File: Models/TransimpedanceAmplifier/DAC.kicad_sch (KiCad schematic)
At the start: 11 parts, among them U10 DAC81401

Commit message: Finalized the last detail of the schematic
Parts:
- renumbered R17 to R18
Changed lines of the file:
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@@
 		(dnp no)
 		(fields_autoplaced yes)
-		(property "Reference" "R17"
+		(property "Reference" "R18"
 			(at 143.51 36.83 90)
 			(effects
@@
 			(project ""
 				(path "/ec9f2ae3-e40d-40eb-9760-2b611ee8efd1/7e303428-a18c-4ad4-b002-5ab9c6631588/77c98efe-b6d0-43b4-bfa9-b392bfbf9a85"
-					(reference "R17")
+					(reference "R18")
 					(unit 1)
 				)

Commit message: Working on filling in the last details of the schematics
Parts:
- C25, C26, C27, C28, C29: footprint (none) -> TwoTerminal:CAPC0603; Cost (none) -> $0.00; RoHS Compliant (none) -> NO
- NT1, NT2, NT3, NT4, R18, U10: Cost (none) -> $0.00; RoHS Compliant (none) -> NO
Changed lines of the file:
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@@
 			)
 		)
-		(property "Footprint" ""
+		(property "Footprint" "TwoTerminal:CAPC0603"
 			(at 51.7652 114.3 0)
 			(effects
@@
 		)
 		(property "Purchase Link" "https://www.digikey.com/en/products/detail/murata-electronics/GRT188R61H105KE13D/5416752"
+			(at 50.8 110.49 0)
+			(effects
+				(font
+					(size 1.27 1.27)
+				)
+				(hide yes)
+			)
+		)
+		(property "Cost" "$0.00"
+			(at 50.8 110.49 0)
+			(effects
+				(font
+					(size 1.27 1.27)
+				)
+				(hide yes)
+			)
+		)
+		(property "RoHS Compliant" "NO"
 			(at 50.8 110.49 0)
 			(effects
@@
 			)
 		)
-		(property "Footprint" ""
+		(property "Footprint" "TwoTerminal:CAPC0603"
 			(at 127.9652 165.1 0)
 			(effects
@@
 		)
 		(property "Purchase Link" "https://www.digikey.com/en/products/detail/murata-electronics/GRT188R61H105KE13D/5416752"
+			(at 127 161.29 0)
+			(effects
+				(font
+					(size 1.27 1.27)
+				)
+				(hide yes)
+			)
+		)
+		(property "Cost" "$0.00"
+			(at 127 161.29 0)
+			(effects
+				(font
+					(size 1.27 1.27)
+				)
+				(hide yes)
+			)
+		)
+		(property "RoHS Compliant" "NO"
 			(at 127 161.29 0)
 			(effects
@@
 			)
 		)
+		(property "Cost" "$0.00"
+			(at 58.42 152.4 0)
+			(effects
+				(font
+					(size 1.27 1.27)
+				)
+				(hide yes)
+			)
+		)
+		(property "RoHS Compliant" "NO"
+			(at 58.42 152.4 0)
+			(effects
+				(font
+					(size 1.27 1.27)
+				)
+				(hide yes)
+			)
+		)
 		(pin "2"
 		)
@@
 			)
 		)
-		(property "Footprint" ""
+		(property "Footprint" "TwoTerminal:CAPC0603"
 			(at 127.9652 114.3 0)
 			(effects
@@
 		)
 		(property "Purchase Link" "https://www.digikey.com/en/products/detail/murata-electronics/GRT188R61H105KE13D/5416752"
+			(at 127 110.49 0)
+			(effects
+				(font
+					(size 1.27 1.27)
+				)
+				(hide yes)
+			)
+		)
+		(property "Cost" "$0.00"
+			(at 127 110.49 0)
+			(effects
+				(font
+					(size 1.27 1.27)
+				)
+				(hide yes)
+			)
+		)
+		(property "RoHS Compliant" "NO"
 			(at 127 110.49 0)
 			(effects
@@
 			)
 		)
+		(property "Cost" "$0.00"
+			(at 143.51 43.18 90)
+			(effects
+				(font
+					(size 1.27 1.27)
+				)
+				(hide yes)
+			)
+		)
+		(property "RoHS Compliant" "NO"
+			(at 143.51 43.18 90)
+			(effects
+				(font
+					(size 1.27 1.27)
+				)
+				(hide yes)
+			)
+		)
 		(pin "1"
 		)
@@
 			)
 		)
+		(property "Cost" "$0.00"
+			(at 58.42 101.6 0)
+			(effects
+				(font
+					(size 1.27 1.27)
+				)
+				(hide yes)
+			)
+		)
+		(property "RoHS Compliant" "NO"
+			(at 58.42 101.6 0)
+			(effects
+				(font
+					(size 1.27 1.27)
+				)
+				(hide yes)
+			)
+		)
 		(pin "2"
 		)
@@
 			)
 		)
+		(property "Cost" "$0.00"
+			(at 134.62 152.4 0)
+			(effects
+				(font
+					(size 1.27 1.27)
+				)
+				(hide yes)
+			)
+		)
+		(property "RoHS Compliant" "NO"
+			(at 134.62 152.4 0)
+			(effects
+				(font
+					(size 1.27 1.27)
+				)
+				(hide yes)
+			)
+		)
 		(pin "2"
 		)
@@
 			)
 		)
-		(property "Footprint" ""
+		(property "Footprint" "TwoTerminal:CAPC0603"
 			(at 44.1452 53.34 0)
 			(effects
@@
 		)
 		(property "Purchase Link" "https://www.digikey.com/en/products/detail/murata-electronics/GRM188R71H224KAC4D/5797498"
+			(at 43.18 49.53 0)
+			(effects
+				(font
+					(size 1.27 1.27)
+				)
+				(hide yes)
+			)
+		)
+		(property "Cost" "$0.00"
+			(at 43.18 49.53 0)
+			(effects
+				(font
+					(size 1.27 1.27)
+				)
+				(hide yes)
+			)
+		)
+		(property "RoHS Compliant" "NO"
 			(at 43.18 49.53 0)
 			(effects
@@
 			)
 		)
+		(property "Cost" "$0.00"
+			(at 134.62 101.6 0)
+			(effects
+				(font
+					(size 1.27 1.27)
+				)
+				(hide yes)
+			)
+		)
+		(property "RoHS Compliant" "NO"
+			(at 134.62 101.6 0)
+			(effects
+				(font
+					(size 1.27 1.27)
+				)
+				(hide yes)
+			)
+		)
 		(pin "1"
 		)
@@
 			)
 		)
+		(property "Cost" "$0.00"
+			(at 72.39 30.48 0)
+			(effects
+				(font
+					(size 1.27 1.27)
+				)
+				(hide yes)
+			)
+		)
+		(property "RoHS Compliant" "NO"
+			(at 72.39 30.48 0)
+			(effects
+				(font
+					(size 1.27 1.27)
+				)
+				(hide yes)
+			)
+		)
 		(pin "13"
 		)
@@
 			)
 		)
-		(property "Footprint" ""
+		(property "Footprint" "TwoTerminal:CAPC0603"
 			(at 51.7652 165.1 0)
 			(effects
@@
 			(at 50.8 161.29 0)
 			(effects
+				(font
+					(size 1.27 1.27)
+				)
+				(hide yes)
+			)
+		)
+		(property "Cost" "$0.00"
+			(at 50.8 161.29 0)
+			(effects
+				(font
+					(size 1.27 1.27)
+				)
+				(hide yes)
+			)
+		)
+		(property "RoHS Compliant" "NO"
+			(at 50.8 161.29 0)
+			(effects

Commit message: Fixed a bug in footprint assignment
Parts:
- NT1, NT2, NT3, NT4: footprint (none) -> Connector_Custom:NetTie_0.2mm
- R18: footprint (none) -> TwoTerminal:RESC0603
- U10: footprint (none) -> IC:DAC81401
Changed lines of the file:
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@@
 			)
 		)
-		(property "Footprint" ""
+		(property "Footprint" "Connector_Custom:NetTie_0.2mm"
 			(at 58.42 152.4 0)
 			(effects
@@
 			)
 		)
-		(property "Footprint" ""
+		(property "Footprint" "TwoTerminal:RESC0603"
 			(at 143.764 42.164 90)
 			(effects
@@
 			)
 		)
-		(property "Footprint" ""
+		(property "Footprint" "Connector_Custom:NetTie_0.2mm"
 			(at 58.42 101.6 0)
 			(effects
@@
 			)
 		)
-		(property "Footprint" ""
+		(property "Footprint" "Connector_Custom:NetTie_0.2mm"
 			(at 134.62 152.4 0)
 			(effects
@@
 			)
 		)
-		(property "Footprint" ""
+		(property "Footprint" "Connector_Custom:NetTie_0.2mm"
 			(at 134.62 101.6 0)
 			(effects
@@
 			)
 		)
-		(property "Footprint" ""
+		(property "Footprint" "IC:DAC81401"
 			(at 72.39 30.48 0)
 			(effects

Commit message: Save progress
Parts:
- C25, C26, C27, C28, C29: Cost $0.00 -> $0.14; Cost (qty10) (none) -> $0.078; RoHS Compliant NO -> YES
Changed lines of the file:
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@@
 			)
 		)
-		(property "Cost" "$0.00"
+		(property "Cost" "$0.14"
 			(at 50.8 110.49 0)
 			(effects
@@
 			)
 		)
-		(property "RoHS Compliant" "NO"
+		(property "RoHS Compliant" "YES"
+			(at 50.8 110.49 0)
+			(effects
+				(font
+					(size 1.27 1.27)
+				)
+				(hide yes)
+			)
+		)
+		(property "Cost (qty10)" "$0.078"
 			(at 50.8 110.49 0)
 			(effects
@@
 			)
 		)
-		(property "Cost" "$0.00"
+		(property "Cost" "$0.14"
 			(at 127 161.29 0)
 			(effects
@@
 			)
 		)
-		(property "RoHS Compliant" "NO"
+		(property "RoHS Compliant" "YES"
+			(at 127 161.29 0)
+			(effects
+				(font
+					(size 1.27 1.27)
+				)
+				(hide yes)
+			)
+		)
+		(property "Cost (qty10)" "$0.078"
 			(at 127 161.29 0)
 			(effects
@@
 			)
 		)
-		(property "Cost" "$0.00"
+		(property "Cost" "$0.14"
 			(at 127 110.49 0)
 			(effects
@@
 			)
 		)
-		(property "RoHS Compliant" "NO"
+		(property "RoHS Compliant" "YES"
+			(at 127 110.49 0)
+			(effects
+				(font
+					(size 1.27 1.27)
+				)
+				(hide yes)
+			)
+		)
+		(property "Cost (qty10)" "$0.078"
 			(at 127 110.49 0)
 			(effects
@@
 			)
 		)
-		(property "Cost" "$0.00"
+		(property "Cost" "$0.14"
 			(at 43.18 49.53 0)
 			(effects
@@
 			)
 		)
-		(property "RoHS Compliant" "NO"
+		(property "RoHS Compliant" "YES"
+			(at 43.18 49.53 0)
+			(effects
+				(font
+					(size 1.27 1.27)
+				)
+				(hide yes)
+			)
+		)
+		(property "Cost (qty10)" "$0.078"
 			(at 43.18 49.53 0)
 			(effects
@@
 			)
 		)
-		(property "Cost" "$0.00"
+		(property "Cost" "$0.14"
 			(at 50.8 161.29 0)
 			(effects
@@
 			)
 		)
-		(property "RoHS Compliant" "NO"
+		(property "RoHS Compliant" "YES"
 			(at 50.8 161.29 0)
 			(effects
+				(font
+					(size 1.27 1.27)
+				)
+				(hide yes)
+			)
+		)
+		(property "Cost (qty10)" "$0.078"
+			(at 50.8 161.29 0)
+			(effects

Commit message: Almost done with generating bill of materials
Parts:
- NT1, NT2, NT3, NT4: Cost $0.00 -> (none); RoHS Compliant NO -> (none)
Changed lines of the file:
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@@
 			)
 		)
-		(property "Cost" "$0.00"
+		(property "Cost" ""
 			(at 58.42 152.4 0)
 			(effects
@@
 			)
 		)
-		(property "RoHS Compliant" "NO"
+		(property "RoHS Compliant" ""
 			(at 58.42 152.4 0)
 			(effects
@@
 			)
 		)
-		(property "Cost" "$0.00"
+		(property "Cost" ""
 			(at 58.42 101.6 0)
 			(effects
@@
 			)
 		)
-		(property "RoHS Compliant" "NO"
+		(property "RoHS Compliant" ""
 			(at 58.42 101.6 0)
 			(effects
@@
 			)
 		)
-		(property "Cost" "$0.00"
+		(property "Cost" ""
 			(at 134.62 152.4 0)
 			(effects
@@
 			)
 		)
-		(property "RoHS Compliant" "NO"
+		(property "RoHS Compliant" ""
 			(at 134.62 152.4 0)
 			(effects
@@
 			)
 		)
-		(property "Cost" "$0.00"
+		(property "Cost" ""
 			(at 134.62 101.6 0)
 			(effects
@@
 			)
 		)
-		(property "RoHS Compliant" "NO"
+		(property "RoHS Compliant" ""
 			(at 134.62 101.6 0)
 			(effects

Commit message: Going to shift all the expensive, hard-to-find ICs over to Mouser
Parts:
- R18: Cost $0.00 -> $0.10; Cost (qty10) (none) -> $0.030; RoHS Compliant NO -> YES
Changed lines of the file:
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@@
 			)
 		)
-		(property "Cost" "$0.00"
+		(property "Cost" "$0.10"
 			(at 143.51 43.18 90)
 			(effects
@@
 			)
 		)
-		(property "RoHS Compliant" "NO"
+		(property "RoHS Compliant" "YES"
 			(at 143.51 43.18 90)
 			(effects
+				(font
+					(size 1.27 1.27)
+				)
+				(hide yes)
+			)
+		)
+		(property "Cost (qty10)" "$0.030"
+			(at 143.51 43.18 90)
+			(effects

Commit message: Exclude these pin headers from the BOM; they are just cheap breakaway pins
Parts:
- U10: Cost $0.00 -> $14.10; Cost (qty10) (none) -> $11.124; RoHS Compliant NO -> YES
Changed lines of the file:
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@@
 			)
 		)
-		(property "Cost" "$0.00"
+		(property "Cost" "$14.10"
 			(at 72.39 30.48 0)
 			(effects
@@
 			)
 		)
-		(property "RoHS Compliant" "NO"
+		(property "RoHS Compliant" "YES"
 			(at 72.39 30.48 0)
 			(effects
+				(font
+					(size 1.27 1.27)
+				)
+				(hide yes)
+			)
+		)
+		(property "Cost (qty10)" "$11.124"
+			(at 72.39 30.48 0)
+			(effects

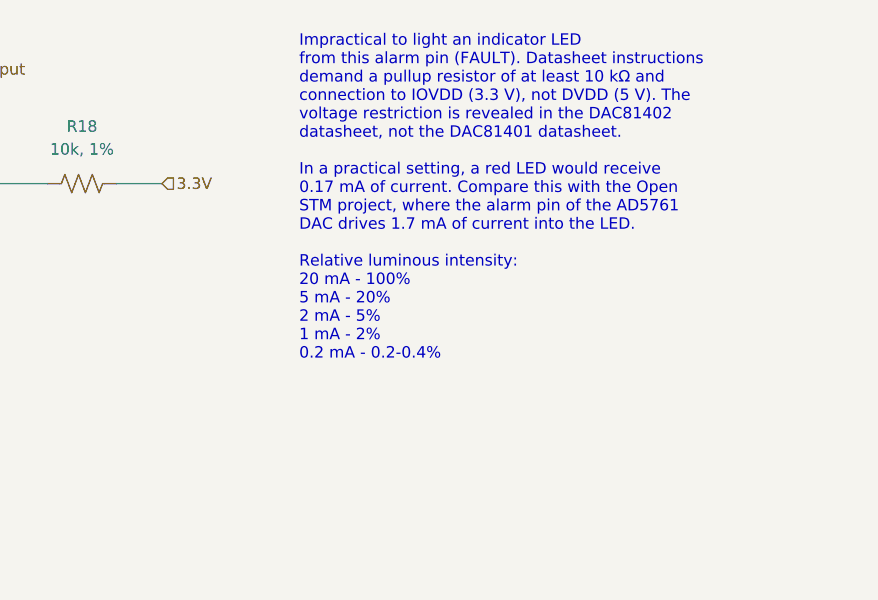
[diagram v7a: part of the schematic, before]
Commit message: Revised connectivity to improve physical layout
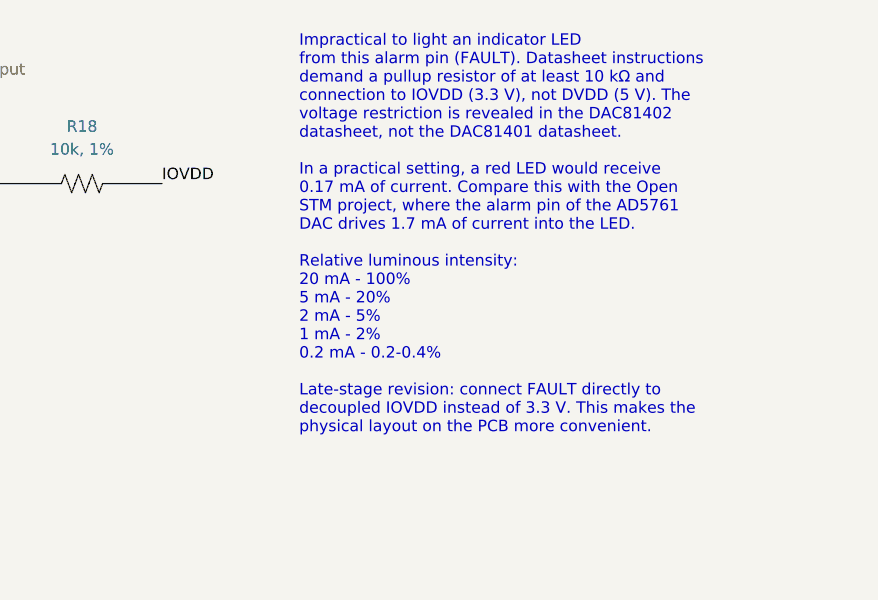
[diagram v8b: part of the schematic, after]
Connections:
- net 3.3V: no longer R18.2
- net IOVDD: now also R18.2
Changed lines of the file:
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@@
 	(generator_version "9.0")
 	(paper "A4")
-	(text "Impractical to light an indicator LED\nfrom this alarm pin (FAULT). Datasheet instructions\ndemand a pullup resistor of at least 10 kΩ and\nconnection to IOVDD (3.3 V), not DVDD (5 V). The\nvoltage restriction is revealed in the DAC81402\ndatasheet, not the DAC81401 datasheet.\n\nIn a practical setting, a red LED would receive\n0.17 mA of current. Compare this with the Open\nSTM project, where the alarm pin of the AD5761\nDAC drives 1.7 mA of current into the LED.\n\nRelative luminous intensity:\n20 mA - 100%\n5 mA - 20%\n2 mA - 5%\n1 mA - 2%\n0.2 mA - 0.2-0.4%"
+	(text "Impractical to light an indicator LED\nfrom this alarm pin (FAULT). Datasheet instructions\ndemand a pullup resistor of at least 10 kΩ and\nconnection to IOVDD (3.3 V), not DVDD (5 V). The\nvoltage restriction is revealed in the DAC81402\ndatasheet, not the DAC81401 datasheet.\n\nIn a practical setting, a red LED would receive\n0.17 mA of current. Compare this with the Open\nSTM project, where the alarm pin of the AD5761\nDAC drives 1.7 mA of current into the LED.\n\nRelative luminous intensity:\n20 mA - 100%\n5 mA - 20%\n2 mA - 5%\n1 mA - 2%\n0.2 mA - 0.2-0.4%\n\nLate-stage revision: connect FAULT directly to\ndecoupled IOVDD instead of 3.3 V. This makes the\nphysical layout on the PCB more convenient."
 		(exclude_from_sim no)
 		(at 167.64 26.67 0)
@@
 		)
 	)
+	(label "IOVDD"
+		(at 152.4 43.18 0)
+		(effects
+			(font
+				(size 1.27 1.27)
+			)
+			(justify left bottom)
+		)
+	)
 	(label "AVSS"
 		(at 116.84 63.5 0)
@@
 		)
 	)
-	(hierarchical_label "3.3V"
-		(shape input)
-		(at 152.4 43.18 0)
-		(effects
-			(font
-				(size 1.27 1.27)
-			)
-			(justify left)
-		)
-	)
